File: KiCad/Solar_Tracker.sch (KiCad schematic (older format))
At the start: 34 parts

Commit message: made the schematic
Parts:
- removed C?: CP, symbol CP
- added C?: 0.1u, symbol C
- added D? (x3): TVS_x4, symbol TVS_x4
- added D?: TVS_USB, symbol TVS_USB
- added J?: CONN_01X03, symbol CONN_01X03
- added J?: CONN_01X05, symbol CONN_01X05
- added J?: CONN_01X04, symbol CONN_01X04
- added Q? (x4): Q_PMOS_GDSD, symbol Q_PMOS_GDSD
- added Q? (x4): Q_NMOS_DGS, symbol Q_NMOS_DGS
- added R? (x7): R, symbol R
- added SW?: SWITCH, symbol SWITCH
- added SW?: DIPSWITCH, symbol DIPSWITCH
- Y?: value Crystal_GND2 -> 16MHz
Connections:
- net labels added: +48V, AZRTE, ELRATE, EN, ISO_PWR_DET, RECEIVE, TRANSMIT
- wire segments 98 -> 156
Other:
- moved on the sheet: C?, D?, J?, R?, U?, Y?

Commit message: Paula's Changes
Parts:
- added L?: 10 uH, symbol L
- C?: value 0.1uF -> 4.7 uF
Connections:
- net +48V: no longer Q?.2 (D)
- net +5VD: no longer C?.1
- net GND: no longer U?.21 (GND), U?.3 (GND), U?.5 (GND)
- net GNDD: no longer C?.2
- new net: U?.21 (GND), U?.3 (GND), U?.5 (GND)
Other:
- moved on the sheet: C?
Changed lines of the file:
@@
 LIBS:valves
 LIBS:ICs
-LIBS:PASSIVES
 LIBS:Solar_Tracker-cache
 EELAYER 25 0
@@
 L C C?
 U 1 1 59B3EEE2
-P 6050 6350
-F 0 "C?" H 6075 6450 50  0000 L CNN
-F 1 "0.1uF" H 6075 6250 50  0000 L CNN
-F 2 "" H 6088 6200 50  0001 C CNN
-F 3 "" H 6050 6350 50  0001 C CNN
-	1    6050 6350
+P 2500 7250
+F 0 "C?" H 2525 7350 50  0000 L CNN
+F 1 "4.7 uF" H 2525 7150 50  0000 L CNN
+F 2 "" H 2538 7100 50  0001 C CNN
+F 3 "" H 2500 7250 50  0001 C CNN
+	1    2500 7250
 	1    0    0    -1
 $EndComp
@@
 $Comp
 L +5VD #PWR?
-U 1 1 59B40BE2
-P 6050 6200
-F 0 "#PWR?" H 6050 6050 50  0001 C CNN
-F 1 "+5VD" H 6050 6340 50  0000 C CNN
-F 2 "" H 6050 6200 50  0001 C CNN
-F 3 "" H 6050 6200 50  0001 C CNN
-	1    6050 6200
-	1    0    0    -1
-$EndComp
-$Comp
-L +5VD #PWR?
 U 1 1 59B40C14
 P 6050 5200
@@
 L GND #PWR?
 U 1 1 59C41BC8
-P 1050 5950
-F 0 "#PWR?" H 1050 5700 50  0001 C CNN
-F 1 "GND" H 1050 5800 50  0000 C CNN
-F 2 "" H 1050 5950 50  0001 C CNN
-F 3 "" H 1050 5950 50  0001 C CNN
-	1    1050 5950
+P 1150 7350
+F 0 "#PWR?" H 1150 7100 50  0001 C CNN
+F 1 "GND" H 1150 7200 50  0000 C CNN
+F 2 "" H 1150 7350 50  0001 C CNN
+F 3 "" H 1150 7350 50  0001 C CNN
+	1    1150 7350
 	1    0    0    -1
 $EndComp
@@
 L +48V #PWR?
 U 1 1 59C773D1
-P 8250 4250
-F 0 "#PWR?" H 8250 4100 50  0001 C CNN
-F 1 "+48V" H 8250 4390 50  0000 C CNN
-F 2 "" H 8250 4250 50  0001 C CNN
-F 3 "" H 8250 4250 50  0001 C CNN
-	1    8250 4250
+P 1150 7050
+F 0 "#PWR?" H 1150 6900 50  0001 C CNN
+F 1 "+48V" H 1150 7190 50  0000 C CNN
+F 2 "" H 1150 7050 50  0001 C CNN
+F 3 "" H 1150 7050 50  0001 C CNN
+	1    1150 7050
 	1    0    0    -1
 $EndComp
@@
 	8650 4700 8250 4700
 Connection ~ 8250 4700
+$Comp
+L L L?
+U 1 1 59C51BDA
+P 2000 7050
+F 0 "L?" V 1950 7050 50  0000 C CNN
+F 1 "10 uH" V 2075 7050 50  0000 C CNN
+F 2 "" H 2000 7050 50  0001 C CNN
+F 3 "" H 2000 7050 50  0001 C CNN
+	1    2000 7050
+	0    1    1    0
+$EndComp
 $EndSCHEMATC

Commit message: Paula's update for power
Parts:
- added C?: 4.7 uF, symbol C
- added L?: 10 uH, symbol L
- added U? (x2): MER1S4805SC, symbol MER1S4805SC
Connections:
- net +48V: now also U?.1 (+Vin), U?.1 (+Vin)
- net +5V: now also C?.1, L?.1
- net +5VD: now also C?.1, L?.1
- net GND: now also C?.2, U?.21 (GND), U?.3 (GND), U?.5 (GND), C?.2, U?.2 (-Vin), U?.2 (-Vin), U?.4 (-Vout), U?.4 (-Vout)
- net at L?.2: now also U?.6 (+Vout)
- new net: L?.2, U?.6 (+Vout)
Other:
- moved on the sheet: C?, L?

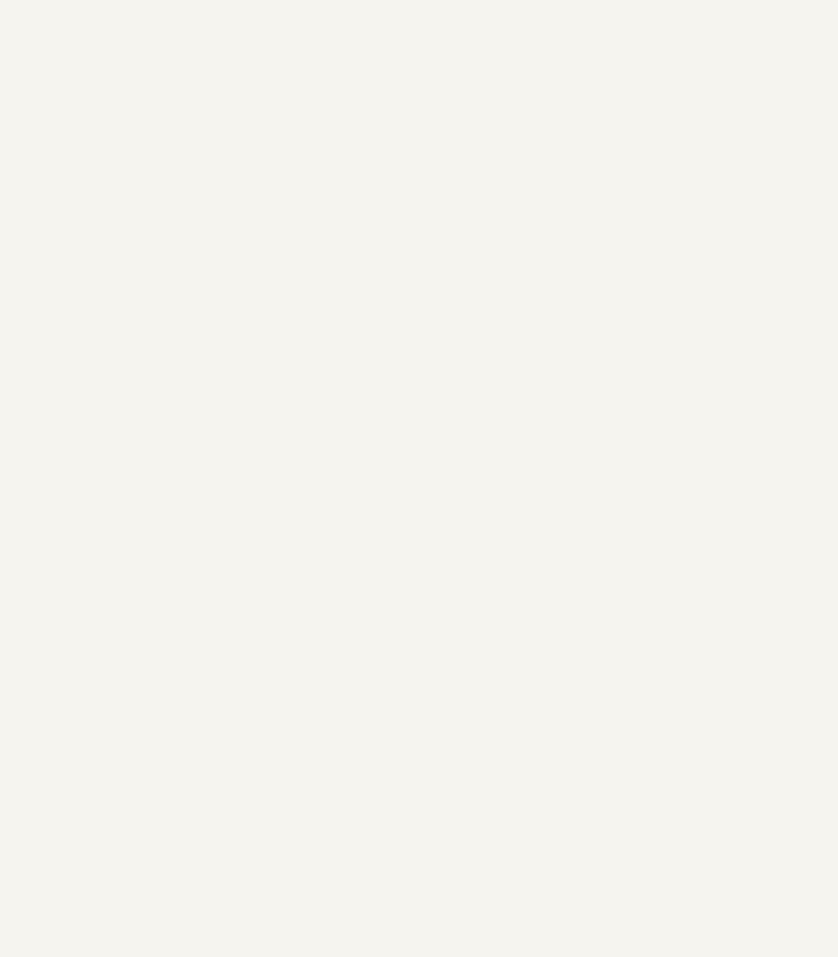
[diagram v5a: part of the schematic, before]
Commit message: Update to add symbol 32U4 to schematic
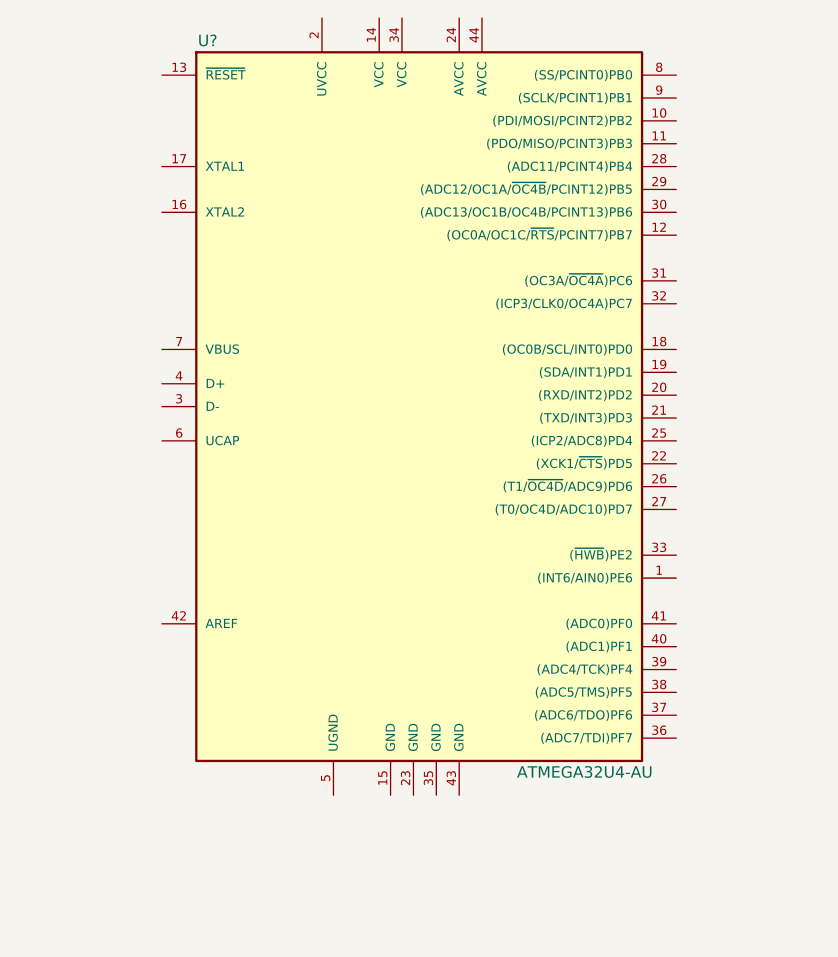
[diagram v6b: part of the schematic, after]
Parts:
- added U?: ATMEGA32U4-AU, TQFP44, symbol ATMEGA32U4-AU
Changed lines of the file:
@@
+	1    0    0    -1
+$EndComp
+$Comp
+L ATMEGA32U4-AU U?
+U 1 1 59C52C86
+P 4850 -1750
+F 0 "U?" H 3900 -50 50  0000 C CNN
+F 1 "ATMEGA32U4-AU" H 5550 -3250 50  0000 C CNN
+F 2 "TQFP44" H 4850 -1750 50  0001 C CIN
+F 3 "" H 5950 -650 50  0001 C CNN
+	1    4850 -1750
 	1    0    0    -1
 $EndComp

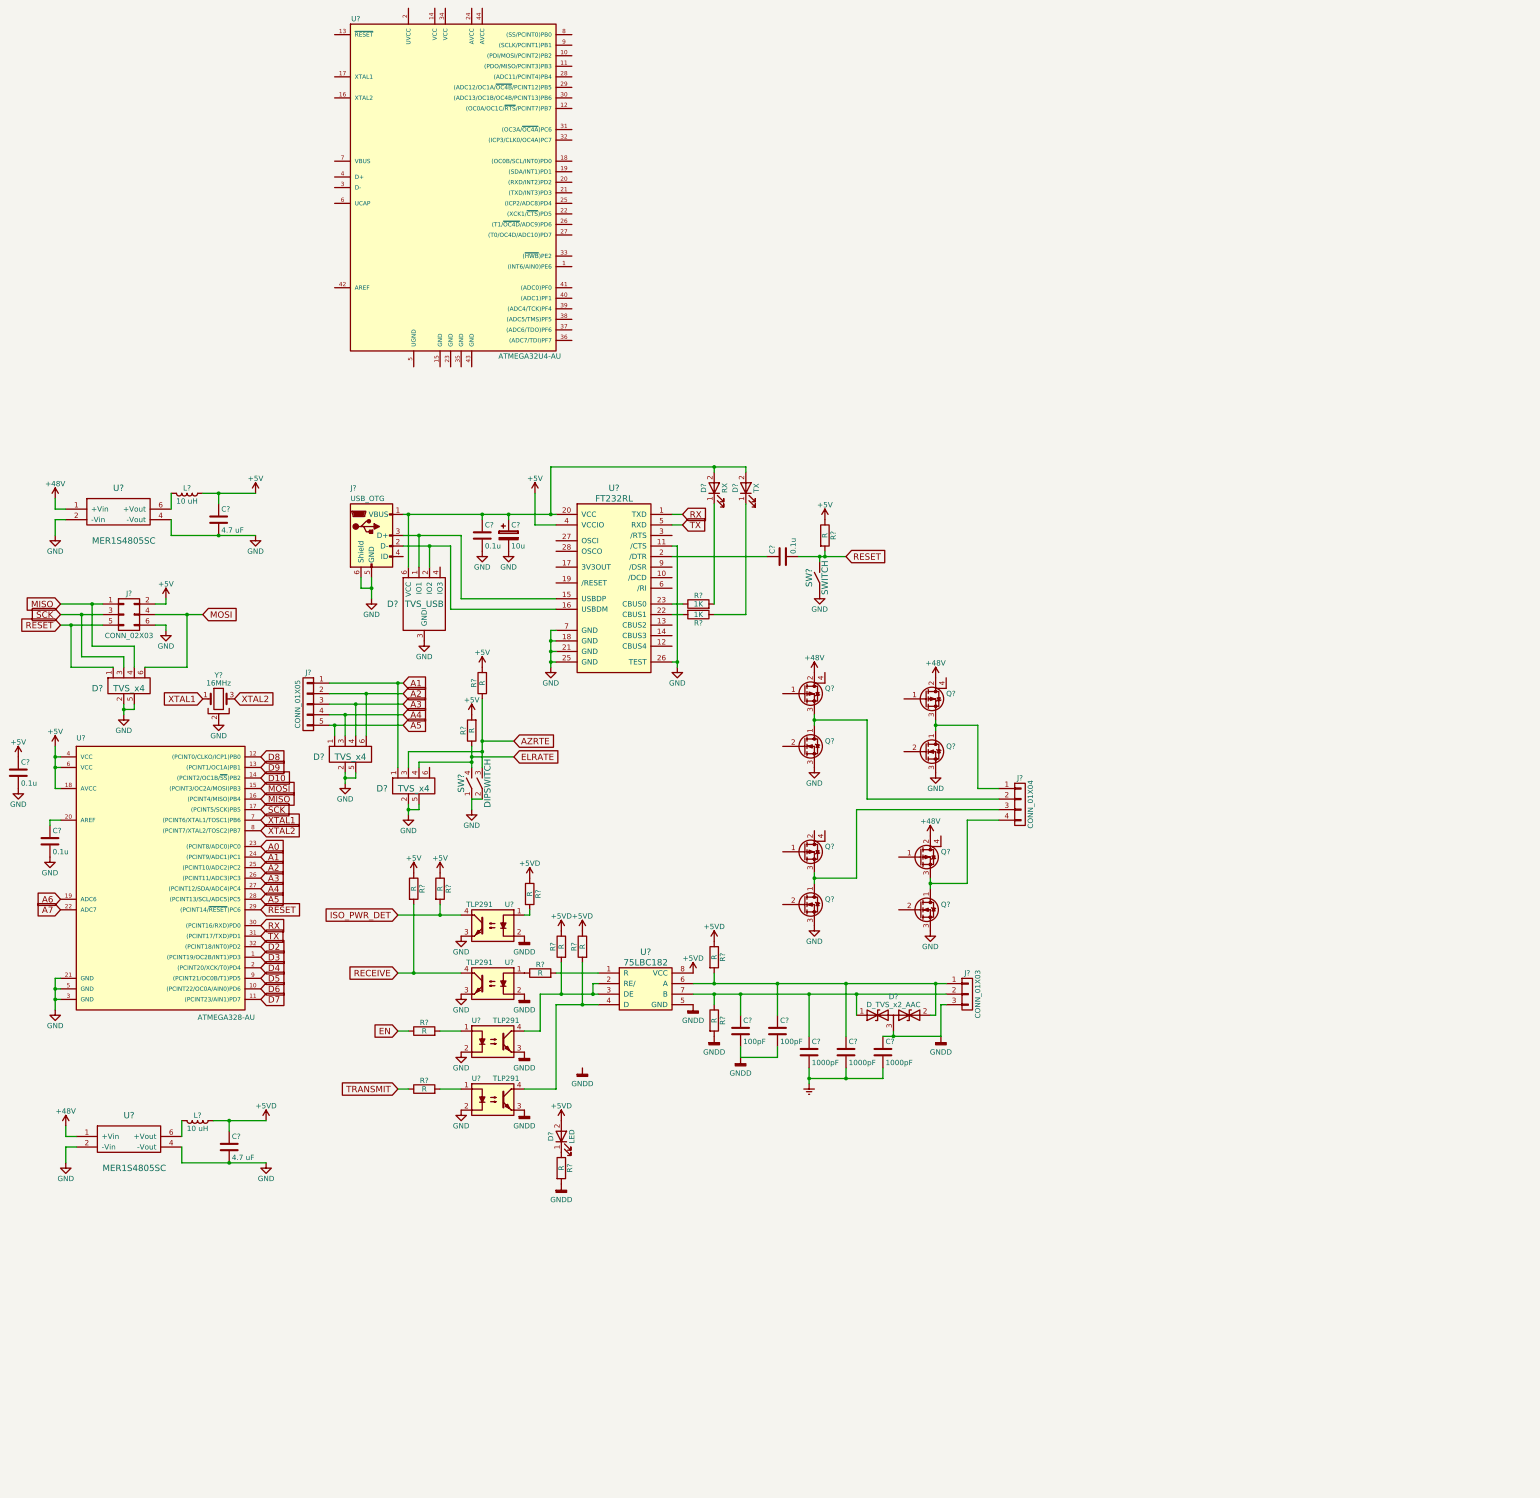
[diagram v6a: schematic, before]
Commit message: Added isolation marking for RS-485
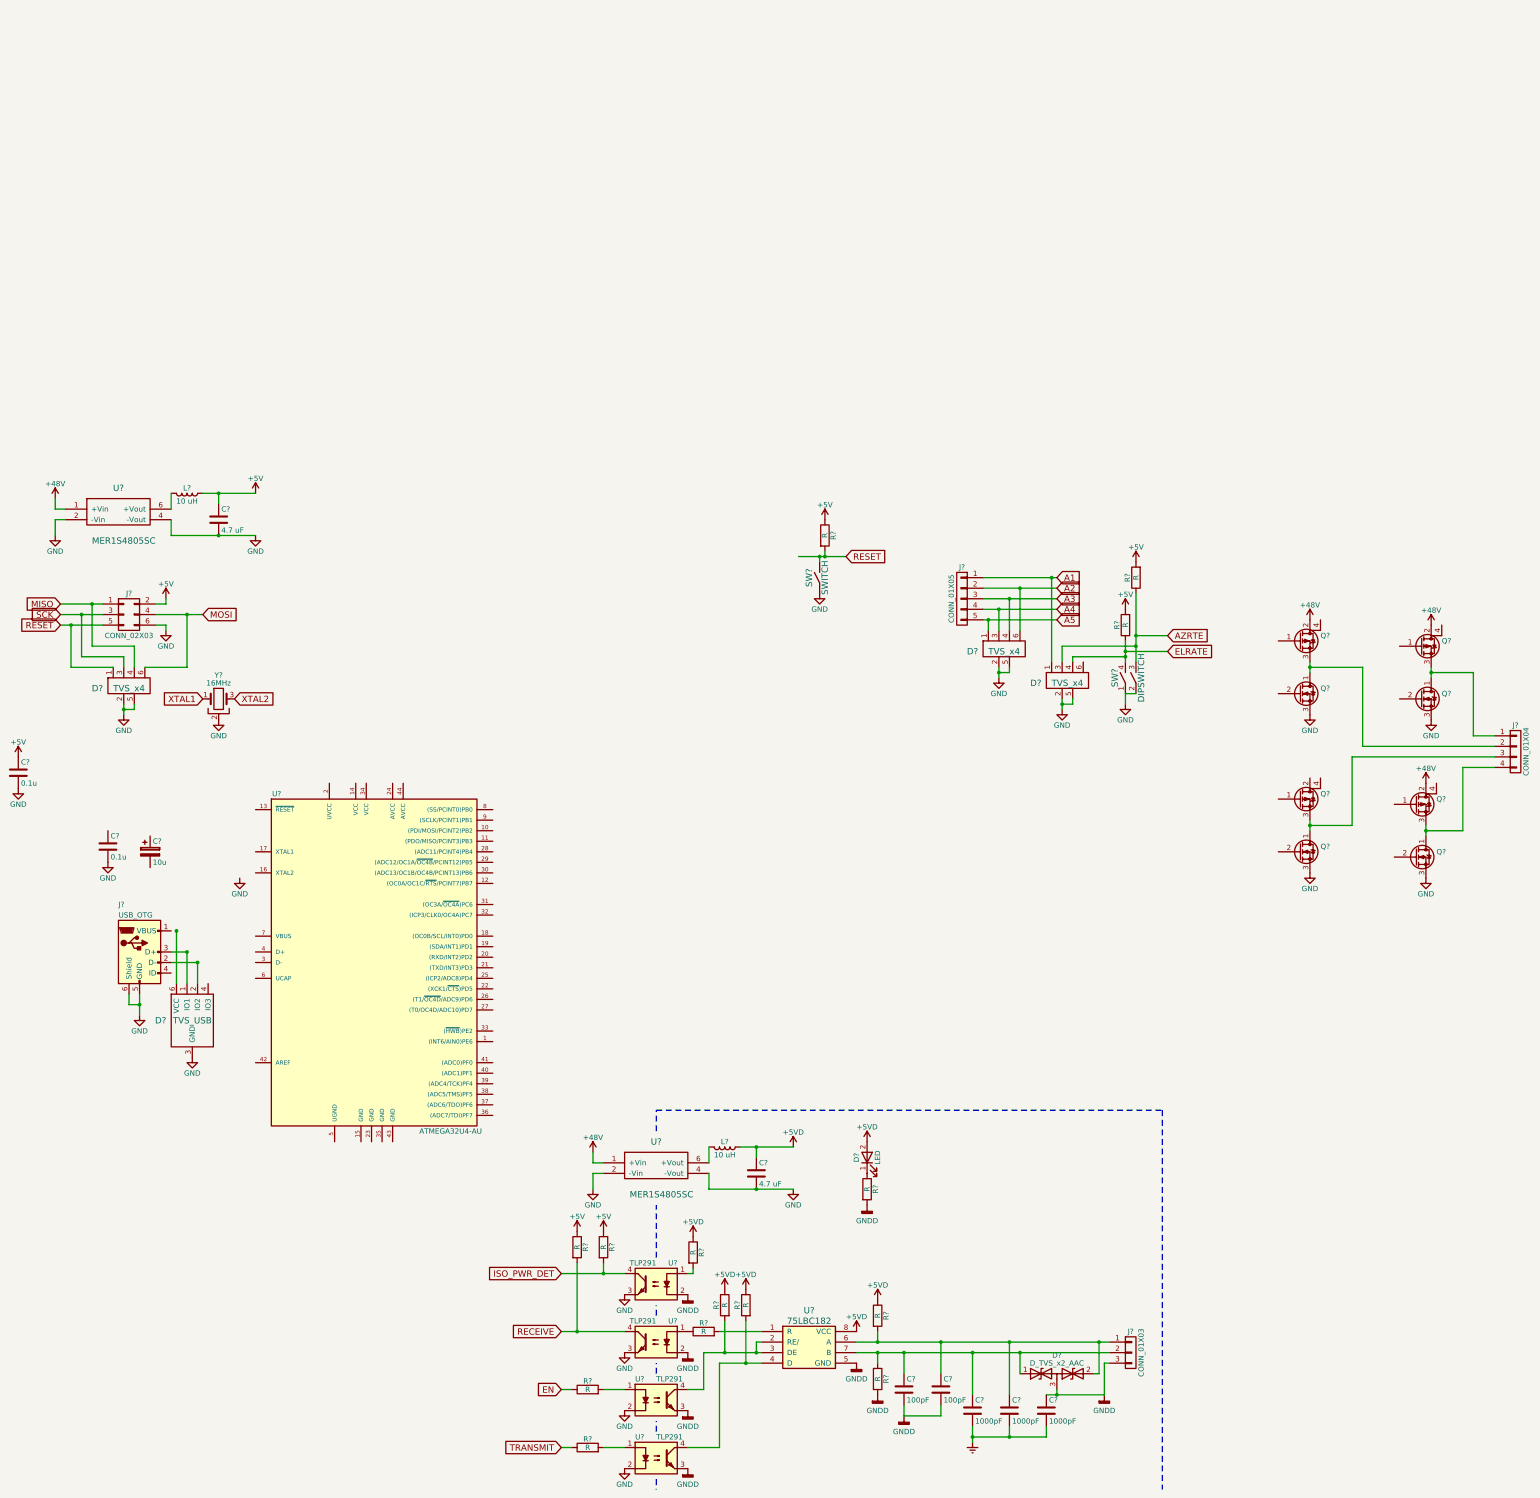
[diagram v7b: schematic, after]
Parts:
- removed C? (x2): 0.1u, symbol C
- removed D?: TX, symbol LED
- removed D?: RX, symbol LED
- removed R? (x2): 1K, symbol R
- removed U?: ATMEGA328-AU, TQFP32, symbol ATMEGA328-AU
- removed U?: FT232RL, symbol FT232RL
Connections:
- net GND: no longer C?.2
- now unconnected: C?.1, C?.1, D?.6 (VCC), J?.1 (VBUS)
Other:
- moved on the sheet: C?, D?, J?, L?, Q?, R?, SW?, U?
